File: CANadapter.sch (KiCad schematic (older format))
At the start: 15 parts

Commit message: added schematic PDF
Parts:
- added P?: CONN_01X06, symbol CONN_01X06
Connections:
- net +3V3: now also P?.6 (P6), P?.6 (P6); no longer P?.5 (P5)
- net +5V: now also P?.6 (P6); no longer P?.5 (P5)
- net GND: now also P?.5 (P5), P?.5 (P5); no longer P?.6 (P6)
- net GNDREF: now also P?.5 (P5); no longer P?.6 (P6)
- net at U?.13 (SCK): now also P?.4 (P4)
- net at U?.14 (MOSI): now also P?.2 (P2)
- net at U?.15 (MISO): now also P?.3 (P3)
- net at U?.16 (CS): now also P?.1 (P1)
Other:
- moved on the sheet: U?
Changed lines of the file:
@@
 LIBS:valves
 LIBS:FabLab
+LIBS:CANadapter-cache
 EELAYER 25 0
 EELAYER END
@@
 encoding utf-8
 Sheet 1 1
-Title ""
-Date ""
-Rev ""
+Title "CAN adapter"
+Date "2016-02-02"
+Rev "0.0"
 Comp ""
 Comment1 ""
@@
 L MCP2515 U?
 U 1 1 56AF4DB4
-P 2000 3650
-F 0 "U?" H 2000 2850 60  0000 C CNN
-F 1 "MCP2515" H 2000 4450 60  0000 C CNN
-F 2 "" H 2050 3400 60  0000 C CNN
-F 3 "" H 2050 3400 60  0000 C CNN
-	1    2000 3650
+P 2450 3650
+F 0 "U?" H 2450 2850 60  0000 C CNN
+F 1 "MCP2515" H 2450 4450 60  0000 C CNN
+F 2 "" H 2500 3400 60  0000 C CNN
+F 3 "" H 2500 3400 60  0000 C CNN
+	1    2450 3650
 	1    0    0    -1
 $EndComp
@@
 L GND #PWR?
 U 1 1 56AF50D5
-P 1250 4550
-F 0 "#PWR?" H 1250 4300 50  0001 C CNN
-F 1 "GND" H 1250 4400 50  0000 C CNN
-F 2 "" H 1250 4550 50  0000 C CNN
-F 3 "" H 1250 4550 50  0000 C CNN
-	1    1250 4550
+P 1700 4550
+F 0 "#PWR?" H 1700 4300 50  0001 C CNN
+F 1 "GND" H 1700 4400 50  0000 C CNN
+F 2 "" H 1700 4550 50  0000 C CNN
+F 3 "" H 1700 4550 50  0000 C CNN
+	1    1700 4550
 	1    0    0    -1
 $EndComp
@@
 $EndComp
 Wire Wire Line
-	1250 4550 1250 4300
-Wire Wire Line
-	1250 4300 1450 4300
+	1700 4550 1700 4300
+Wire Wire Line
+	1700 4300 1900 4300
 $Comp
 L +3.3V #PWR?
 U 1 1 56AF5F1E
-P 3000 4400
-F 0 "#PWR?" H 3000 4250 50  0001 C CNN
-F 1 "+3.3V" H 3000 4540 50  0000 C CNN
-F 2 "" H 3000 4400 50  0000 C CNN
-F 3 "" H 3000 4400 50  0000 C CNN
-	1    3000 4400
-	1    0    0    -1
-$EndComp
-Wire Wire Line
-	3000 4400 3000 4650
-Wire Wire Line
-	3000 4650 2800 4650
-Wire Wire Line
-	2800 4650 2800 4300
-Wire Wire Line
-	2800 4300 2550 4300
+P 3450 4400
+F 0 "#PWR?" H 3450 4250 50  0001 C CNN
+F 1 "+3.3V" H 3450 4540 50  0000 C CNN
+F 2 "" H 3450 4400 50  0000 C CNN
+F 3 "" H 3450 4400 50  0000 C CNN
+	1    3450 4400
+	1    0    0    -1
+$EndComp
+Wire Wire Line
+	3450 4400 3450 4650
+Wire Wire Line
+	3450 4650 3250 4650
+Wire Wire Line
+	3250 4650 3250 4300
+Wire Wire Line
+	3250 4300 3000 4300
 $Comp
 L LTV-356T U?
@@
 	4950 4000 4950 3700
 Wire Wire Line
-	4950 3700 2550 3700
-Wire Wire Line
-	2550 3600 4950 3600
+	4950 3700 3000 3700
+Wire Wire Line
+	3000 3600 4950 3600
 Wire Wire Line
 	4950 3600 4950 3500
@@
 L +5V #PWR?
 U 1 1 56AF9082
-P 8600 1600
-F 0 "#PWR?" H 8600 1450 50  0001 C CNN
-F 1 "+5V" H 8600 1740 50  0000 C CNN
-F 2 "" H 8600 1600 50  0000 C CNN
-F 3 "" H 8600 1600 50  0000 C CNN
-	1    8600 1600
-	1    0    0    -1
-$EndComp
-Wire Wire Line
-	8700 1400 9000 1400
-Wire Wire Line
-	9000 1500 8800 1500
-Wire Wire Line
-	8800 1500 8800 1600
+P 8500 1600
+F 0 "#PWR?" H 8500 1450 50  0001 C CNN
+F 1 "+5V" H 8500 1740 50  0000 C CNN
+F 2 "" H 8500 1600 50  0000 C CNN
+F 3 "" H 8500 1600 50  0000 C CNN
+	1    8500 1600
+	1    0    0    -1
+$EndComp
+Wire Wire Line
+	8800 1400 8800 1600
 Wire Wire Line
 	9000 1100 8600 1100
@@
 Text Label 8600 1100 0    60   ~ 0
 CAN_L
-Text Label 2950 3600 0    60   ~ 0
+Text Label 3400 3600 0    60   ~ 0
 CAN_RX
-Text Label 2950 3700 0    60   ~ 0
+Text Label 3400 3700 0    60   ~ 0
 CAN_TX
 Text Label 7500 1000 0    60   ~ 0
@@
 $EndComp
 Wire Wire Line
-	8000 1500 7800 1500
-Wire Wire Line
-	7800 1500 7800 1600
+	7800 1400 7800 1600
 $Comp
 L +3.3V #PWR?
@@
 	7500 1600 7700 1600
 Wire Wire Line
-	7700 1600 7700 1400
-Wire Wire Line
-	7700 1400 8000 1400
-Wire Wire Line
 	7500 1000 8000 1000
 Wire Wire Line
 	8000 1300 7500 1300
 Wire Wire Line
-	8700 1400 8700 1600
-Wire Wire Line
-	8700 1600 8600 1600
+	8700 1600 8500 1600
 Wire Notes Line
 	7300 700  9500 700
@@
 Text Notes 7450 2150 0    60   ~ 0
 The closest approximation to\nPmod CANbus pinouts I found online\nSee: chipKIT pro MX7
+$Comp
+L CONN_01X06 P?
+U 1 1 56AFFE2D
+P 1050 3450
+F 0 "P?" H 1050 3800 50  0000 C CNN
+F 1 "CONN_01X06" V 1150 3450 50  0000 C CNN
+F 2 "" H 1050 3450 50  0000 C CNN
+F 3 "" H 1050 3450 50  0000 C CNN
+	1    1050 3450
+	-1   0    0    -1
+$EndComp
+Wire Wire Line
+	1250 3200 1900 3200
+Wire Wire Line
+	7800 1400 8000 1400
+Wire Wire Line
+	8000 1500 7700 1500
+Wire Wire Line
+	7700 1500 7700 1600
+Wire Wire Line
+	9000 1400 8800 1400
+Wire Wire Line
+	8700 1600 8700 1500
+Wire Wire Line
+	8700 1500 9000 1500
+Wire Wire Line
+	1250 3300 1650 3300
+Wire Wire Line
+	1650 3300 1650 3400
+Wire Wire Line
+	1650 3400 1900 3400
+Wire Wire Line
+	1900 3500 1550 3500
+Wire Wire Line
+	1550 3500 1550 3400
+Wire Wire Line
+	1550 3400 1250 3400
+Wire Wire Line
+	1250 3500 1350 3500
+Wire Wire Line
+	1750 3300 1900 3300
+Wire Wire Line
+	1750 3300 1750 3100
+Wire Wire Line
+	1750 3100 1350 3100
+Wire Wire Line
+	1350 3100 1350 3500
+$Comp
+L GND #PWR?
+U 1 1 56B00AB8
+P 1350 3950
+F 0 "#PWR?" H 1350 3700 50  0001 C CNN
+F 1 "GND" H 1350 3800 50  0000 C CNN
+F 2 "" H 1350 3950 50  0000 C CNN
+F 3 "" H 1350 3950 50  0000 C CNN
+	1    1350 3950
+	1    0    0    -1
+$EndComp
+Wire Wire Line
+	1250 3600 1350 3600
+Wire Wire Line
+	1350 3600 1350 3950
+$Comp
+L +3.3V #PWR?
+U 1 1 56B00C54
+P 1550 3800
+F 0 "#PWR?" H 1550 3650 50  0001 C CNN
+F 1 "+3.3V" H 1550 3940 50  0000 C CNN
+F 2 "" H 1550 3800 50  0000 C CNN
+F 3 "" H 1550 3800 50  0000 C CNN
+	1    1550 3800
+	1    0    0    -1
+$EndComp
+Wire Wire Line
+	1250 3700 1450 3700
+Wire Wire Line
+	1450 3700 1450 3800
+Wire Wire Line
+	1450 3800 1550 3800
 $EndSCHEMATC

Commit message: Changed CAN termination, added resonator and jumpers
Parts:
- removed C?: C, symbol C
- added C? (x2): 18pF, symbol C
- added C? (x2): 1uF, symbol C
- added JP? (x2): Terminate, symbol Jumper_NC_Small
- added JP?: Filter, symbol Jumper_NC_Small
- added JP? (x2): Use MCP2515, symbol Jumper_NC_Small
- added JP?: Line Power, symbol Jumper_NC_Small
- added P?: Power Bridge, symbol CONN_01X06
- added R?: 100, symbol R
- added R?: 330, symbol R
- added Y?: 16MHz, symbol Crystal_Small
- C?: value C -> 4.7nF
- R?: value 4K7 -> 4.7K
- R? (x2): value 100 -> 60
- R?: value 100 -> 330
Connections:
- net labels added: +5VL
- wire segments 88 -> 100
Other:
- note added: "Add external isolating\nsmps modules here"
- note added: "Pmod SPI compatible"
- moved on the sheet: C?, P?, R?

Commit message: Added basic voltage regulator on line side
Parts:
- added U?: 78L05, symbol 78L05
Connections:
- net labels added: +12V
- net labels removed: +5VL
- wire segments 100 -> 115
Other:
- moved on the sheet: JP?, P?

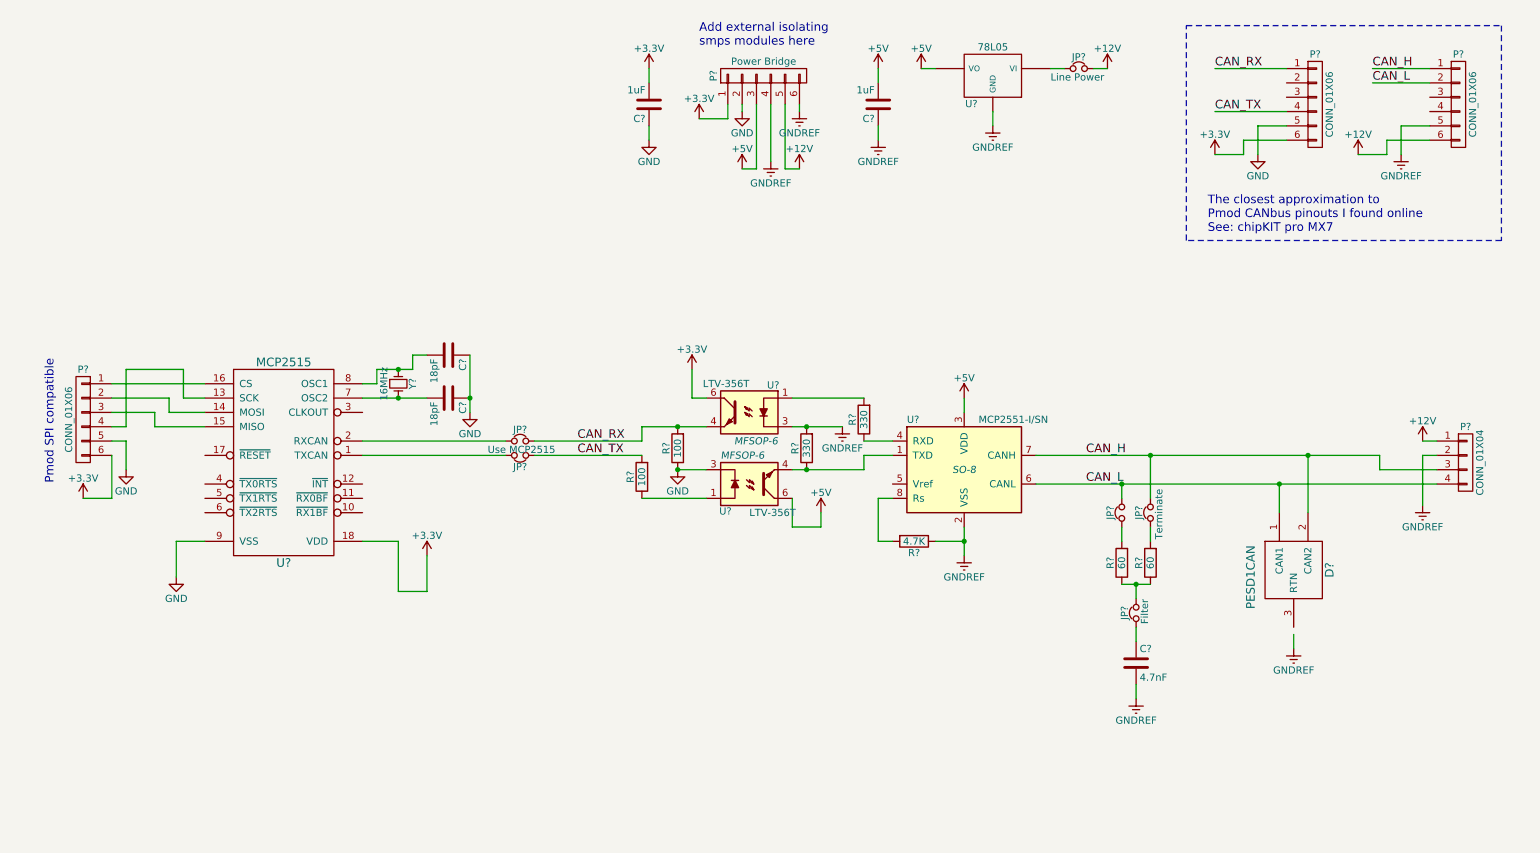
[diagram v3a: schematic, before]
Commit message: Changed CANtx/rx connector, tidied the schematic
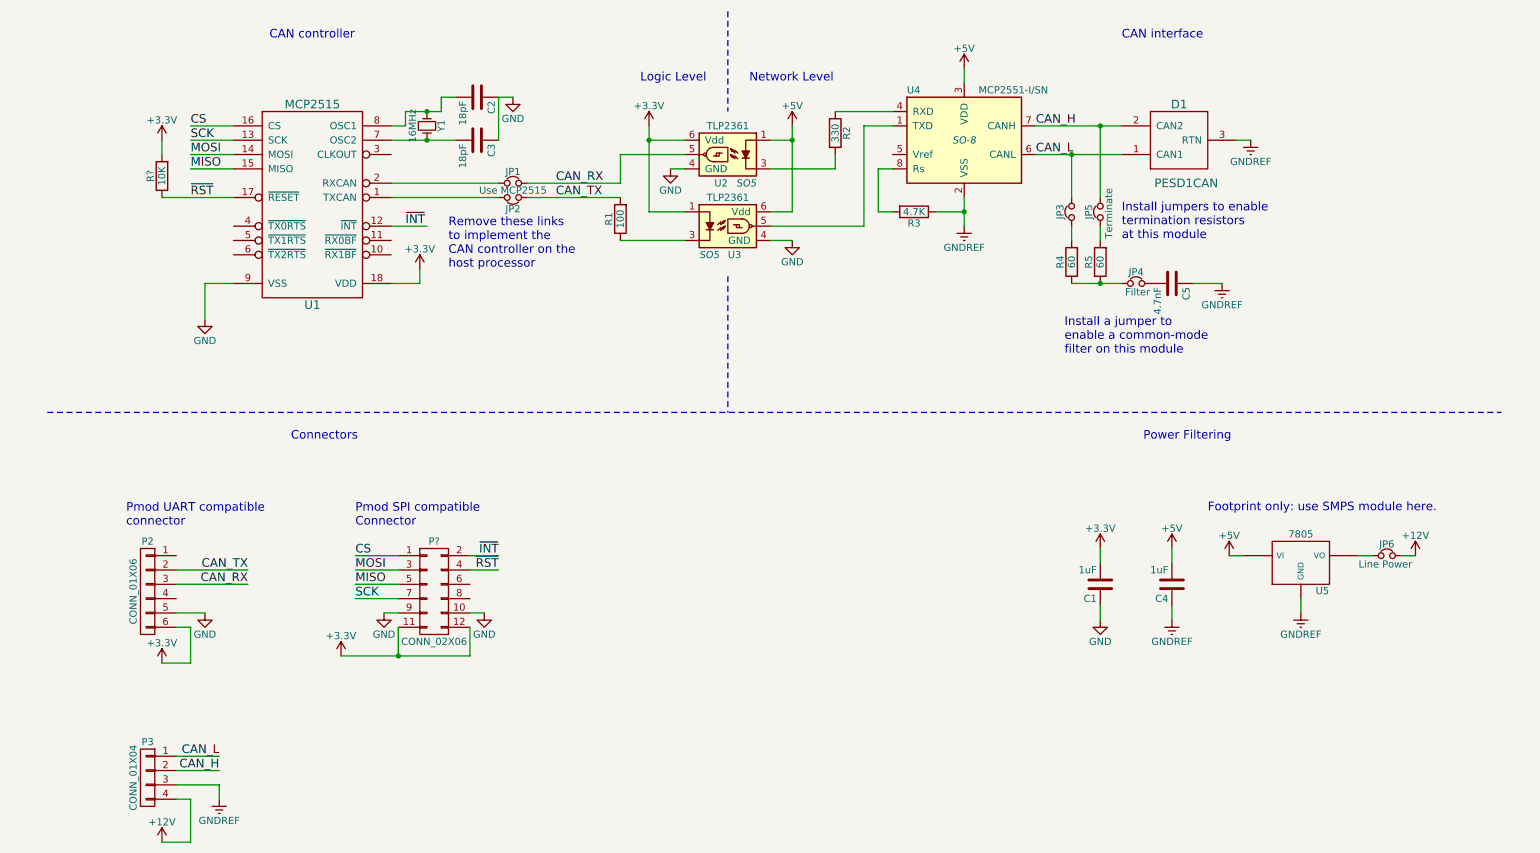
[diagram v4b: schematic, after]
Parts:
- removed P? (x3): CONN_01X06, symbol CONN_01X06
- removed P?: Power Bridge, symbol CONN_01X06
- removed R?: 100, symbol R
- removed R?: 330, symbol R
- removed U? (x2): LTV-356T, MFSOP-6, symbol LTV-356T
- removed U?: 78L05, symbol 78L05
- added P2: CONN_01X06, symbol CONN_01X06
- added P?: CONN_02X06, symbol CONN_02X06
- added R?: 10K, symbol R
- added U2, U3: TLP2361, SO5, symbol TLP2361
- added U5: 7805, symbol 7805
- gave numbers to parts that had none: 21
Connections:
- net +12V: now also P3.4 (P4); no longer P3.1 (P1)
- net +3V3: now also P2.6 (P6), P?.11 (P11), P?.12 (P12), R?.2, U2.6 (Vdd), U3.1
- net +5V: now also U2.1, U3.6 (Vdd), U5.VI
- net CAN_H: now also P3.2 (P2); no longer P3.3 (P3)
- net CAN_L: now also P3.1 (P1); no longer P3.4 (P4)
- net CAN_RX: now also P2.3 (P3), U2.5
- net CAN_TX: now also P2.2 (P2)
- net GND: now also P2.5 (P5), P?.10 (P10), P?.9 (P9), U2.4 (GND), U3.4 (GND)
- net GNDREF: now also C5.1, D1.3 (RTN), P3.3 (P3), U5.GND; no longer C5.2, P3.2 (P2)
- net at U4.1 (TXD): now also U3.5
- net ~INT: now reaches U1.12 (~INT)
- net ~INT: now also P?.2 (P2)
- net SCK: now reaches U1.13 (SCK)
- net SCK: now also P?.7 (P7)
- net MOSI: now reaches U1.14 (MOSI)
- net MOSI: now also P?.3 (P3)
- net MISO: now reaches U1.15 (MISO)
- net MISO: now also P?.5 (P5)
- net CS: now reaches U1.16 (CS)
- net CS: now also P?.1 (P1)
- net ~RST: now reaches U1.17 (~RESET)
- net ~RST: now also P?.4 (P4), R?.1
- net at JP4.1: now also R4.1, R5.1; no longer C5.1
- net at R2.2: now also U2.3
- net at R1.1: now also U3.3
- net at JP6.2: now also U5.VO
- new net: C5.2, JP4.2
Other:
- note added: "CAN controller"
- note added: "CAN interface"
- note added: "Connectors"
- note added: "Footprint only: use SMPS module here."
- note added: "Install a jumper to\nenable a common-mode\nfilter on this module"
- note added: "Install jumpers to enable\ntermination resistors\nat this module"
- note added: "Logic Level"
- note added: "Network Level"
- note added: "Pmod SPI compatible\nConnector"
- note added: "Pmod UART compatible\nconnector"
- note added: "Power Filtering"
- note added: "Remove these links\nto implement the\nCAN controller on the\nhost processor"
- note removed: "Add external isolating\nsmps modules here"
- note removed: "Pmod SPI compatible"
- note removed: "The closest approximation to\nPmod CANbus pinouts I found online\nSee: chipKIT pro MX7"
- moved on the sheet: C1, C2, C3, C4, C5, D1, JP1, JP2, JP3, JP4, JP5, JP6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

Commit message: most footprints associated and roughly placed
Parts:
- C1, C4, C5: footprint (none) -> Capacitors_SMD:C_1206_HandSoldering
- C2, C3: footprint (none) -> Capacitors_SMD:C_0603_HandSoldering
- D1: footprint (none) -> TO_SOT_Packages_SMD:SOT-23_Handsoldering
- P1: renamed from P?; footprint (none) -> Pin_Headers:Pin_Header_Straight_2x06
- P2: footprint (none) -> Pin_Headers:Pin_Header_Straight_1x06
- P3: footprint (none) -> Pin_Headers:Pin_Header_Straight_1x04
- R1, R2, R3: footprint (none) -> Resistors_SMD:R_1210_HandSoldering
- R4, R5: footprint (none) -> Resistors_SMD:R_1218_HandSoldering
- R6: renamed from R?; footprint (none) -> Resistors_SMD:R_1206_HandSoldering
- U1: footprint (none) -> Housings_SOIC:SOIC-18_7.5x11.6mm_Pitch1.27mm
- U2, U3: footprint SO5 -> (none)
- U4: footprint SO-8 -> Power_Integrations:SO-8
- U5: footprint (none) -> TO_SOT_Packages_THT:TO-220_Neutral123_Vertical_LargePads
- Y1: footprint (none) -> Crystals:Crystal_HC49-SD_SMD
